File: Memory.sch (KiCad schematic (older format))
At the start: 26 parts, among them U10 74LS05, U11 74HCT00, U12 74LS27, U13 74HC74, U14 74HC86, U2 AS6C4008-55PCN, U3 AS6C4008-55PCN, U4 AS6C4008-55PCN, U5 AS6C4008-55PCN, U6 74HCT00, U7 74LS32, U8 74LS32, U9 74LS05

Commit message: cleaning up a bit more
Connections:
- net +5V: now also U14.4; no longer JP5.3 (B), U11.12
- net GND: now also U11.12, U11.13; no longer U14.4, U14.5
- net ~RST: now also U14.5; no longer U11.13
- net at U14.6: now also U13.3 (C)
- net at U11.11: no longer U13.3 (C)
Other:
- moved on the sheet: BT1, D1, D2, JP1, JP2, JP3, JP5, JP6, JP7, JP8, R1, U10D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

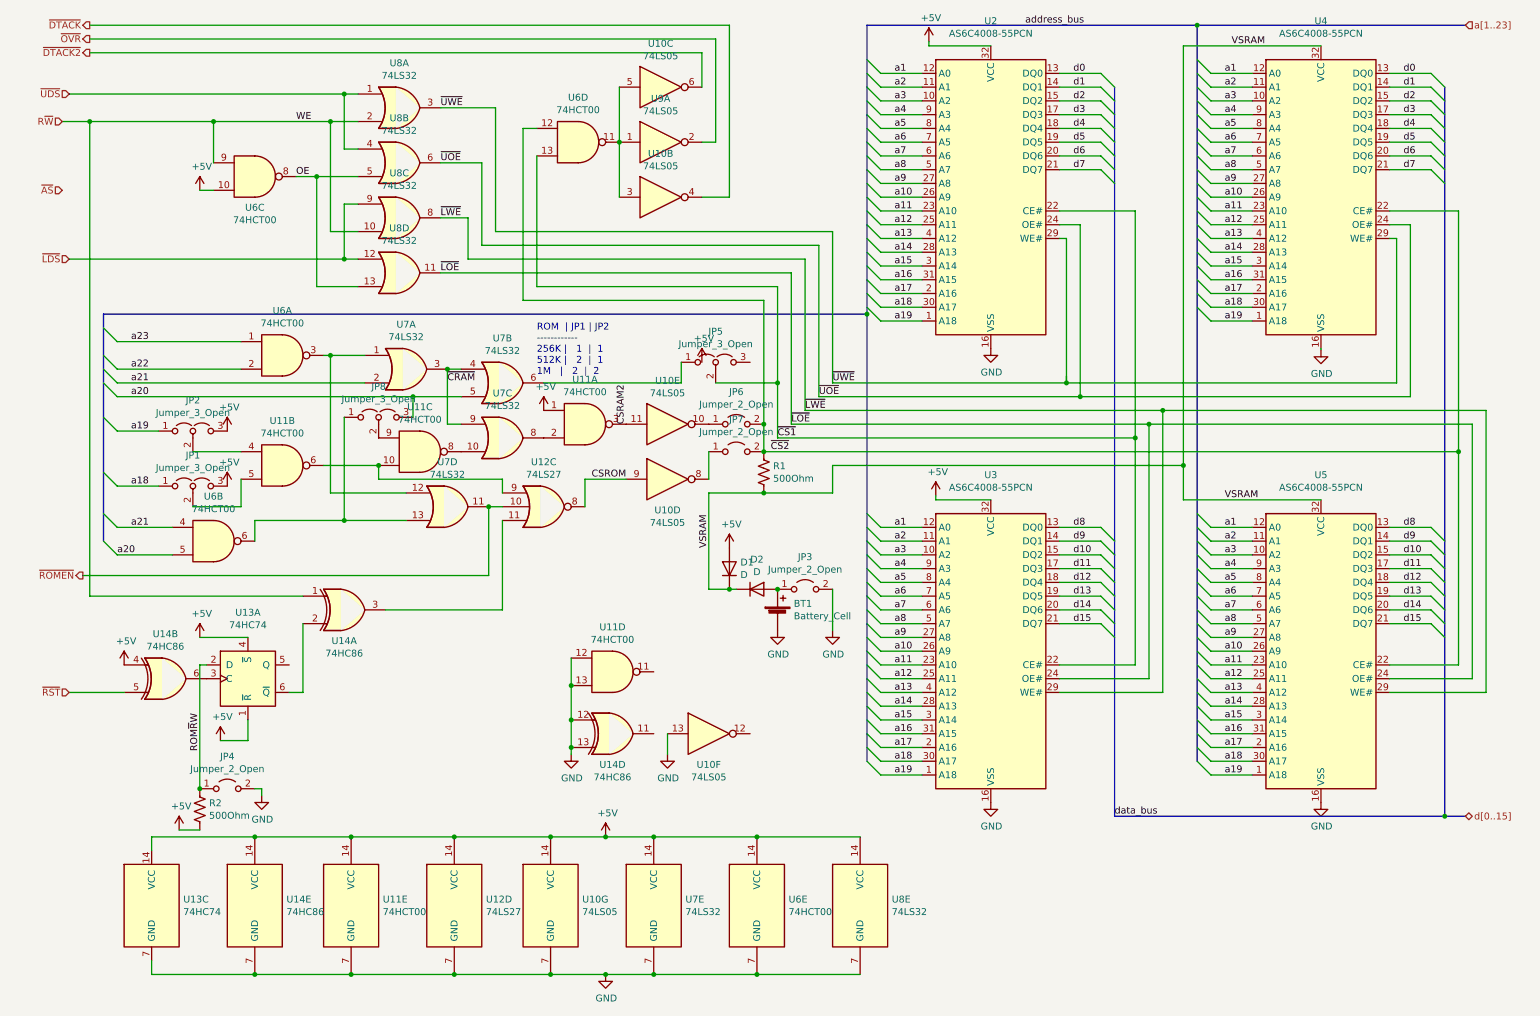
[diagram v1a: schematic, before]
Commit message: finish turbo section
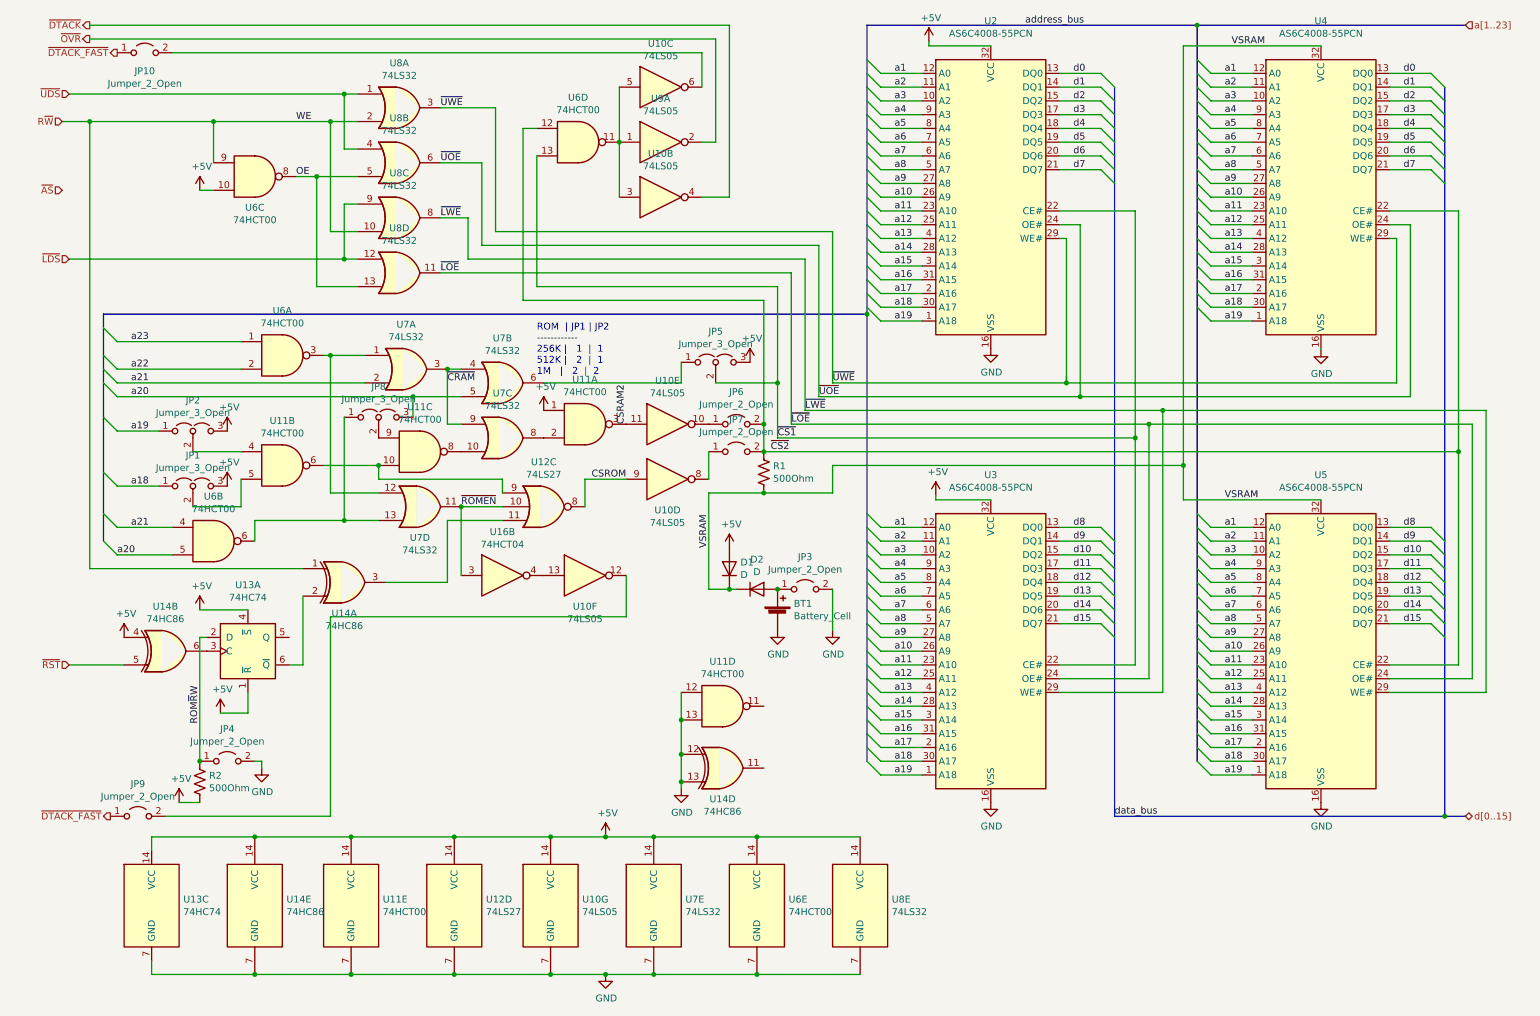
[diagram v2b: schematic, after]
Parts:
- added JP10, JP9: Jumper_2_Open, symbol jumper:Jumper_2_Open
- added U16: 74HCT04, symbol 74:74HCT04
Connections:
- net +5V: now also JP5.3 (B)
- net GND: no longer U10.13
- net ~ROMEN: now also U16.3
- net at U10.12: now also JP9.2 (B)
- net ~DTACK2: no longer names the net of U10.6
- net ~DTACK2: now also JP10.2 (B)
- new net: U10.13, U16.4
- new net ~DTACK_FAST: JP10.1 (A), JP9.1 (A)
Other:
- moved on the sheet: JP4, R2, U10F, U11D, U13A, U14A, U14B, U14D, U7D

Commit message: component names
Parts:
- JP1: value Jumper_3_Open -> 256K_512K
- JP10: value Jumper_2_Open -> Turbo_SRAM
- JP2: value Jumper_3_Open -> 512K_1MB
- JP3: value Jumper_2_Open -> Battery
- JP4: value Jumper_2_Open -> ROMEMUW~R
- JP5: value Jumper_3_Open -> Bank0_ON_OFF
- JP6: value Jumper_2_Open -> Bank1
- JP7: value Jumper_2_Open -> ROMEMU
- JP8: value Jumper_3_Open -> Bank2_C0_D0
- JP9: value Jumper_2_Open -> Turbo_ROM
- R1, R2: value 500Ohm -> 500
- U13: value 74HC74 -> 74HCT74
- U14: value 74HC86 -> 74F86
- U7, U8: value 74LS32 -> 74HCT32
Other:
- note added: "74F is only \nrequired \nfor Turbo"

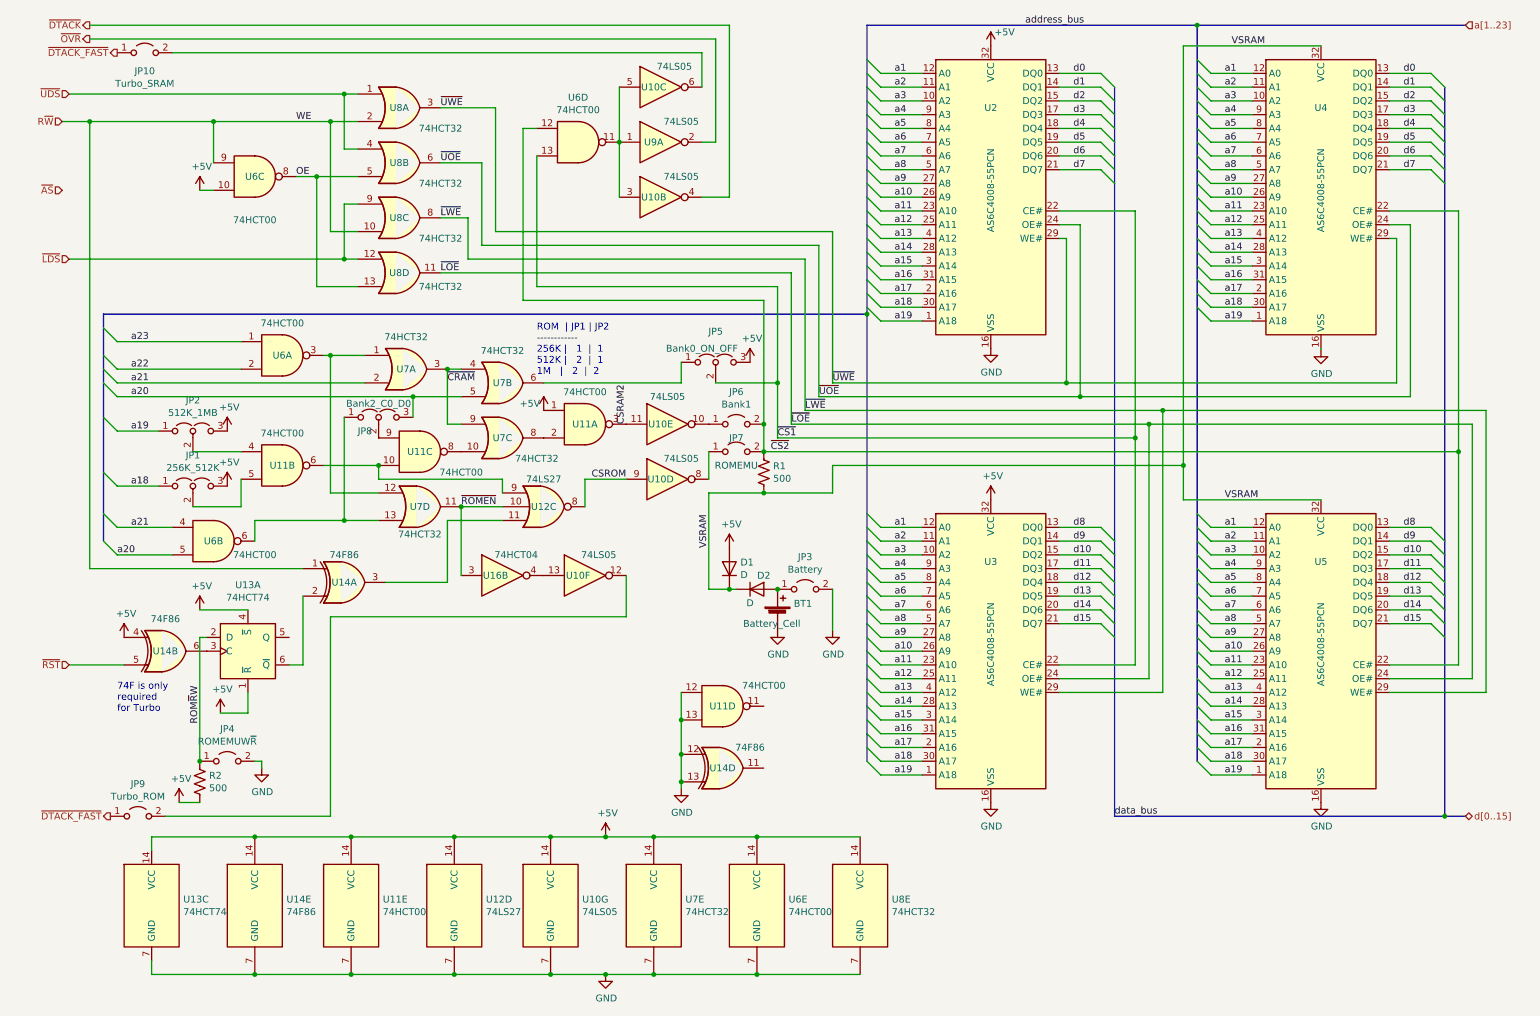
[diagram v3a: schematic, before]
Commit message: capacitors for memory
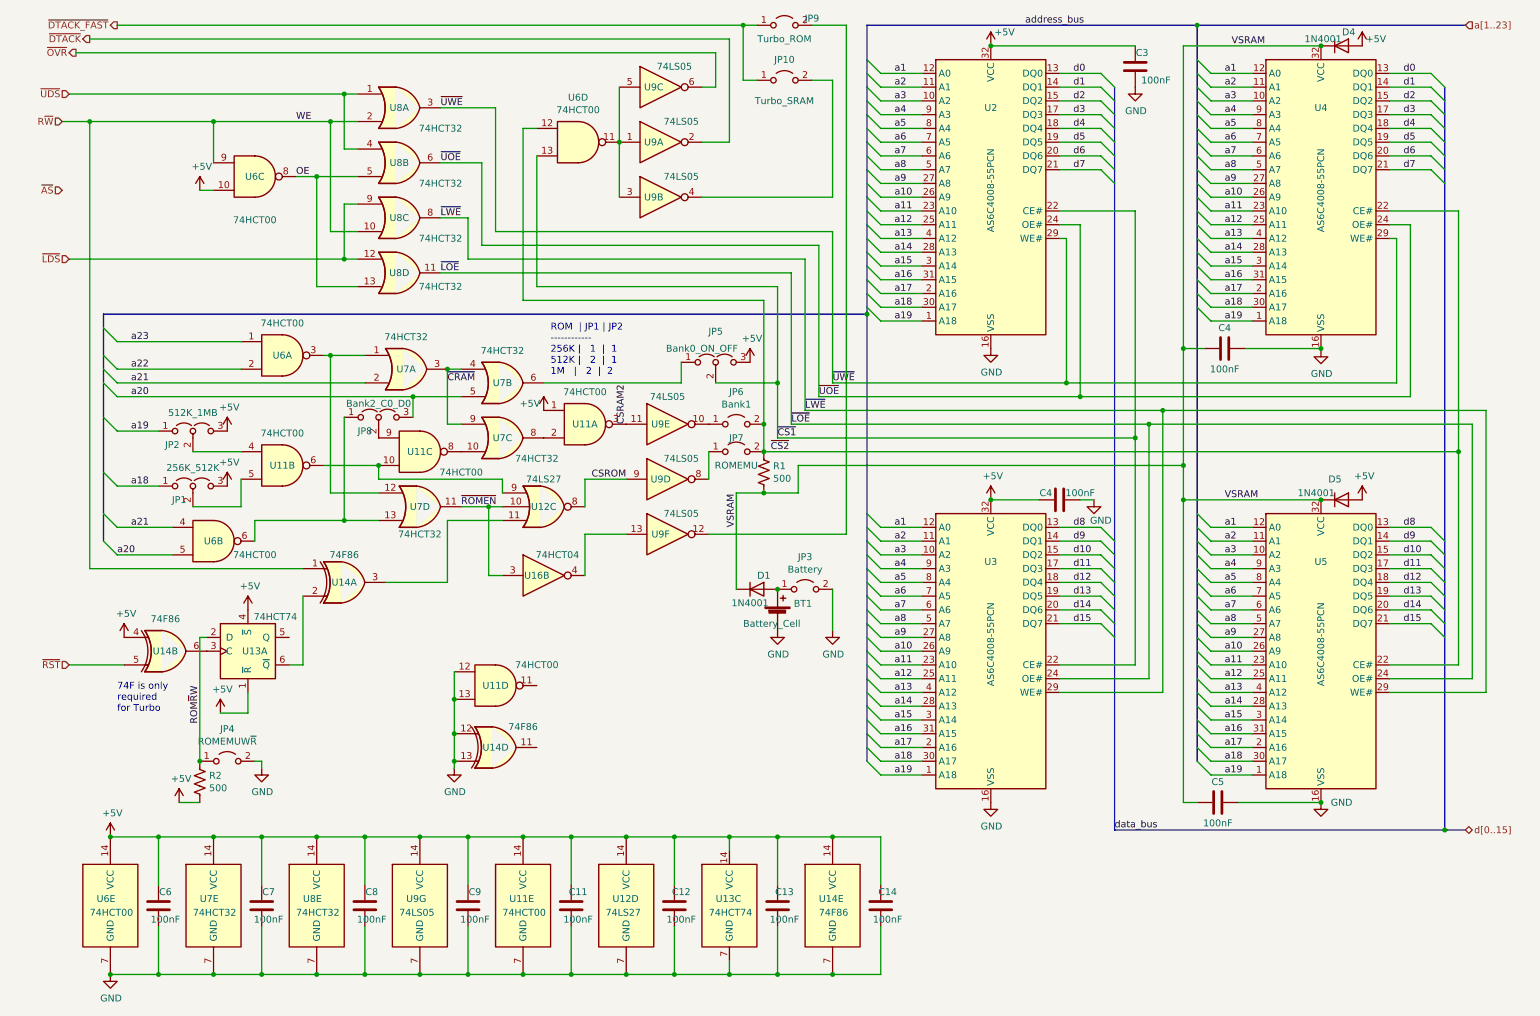
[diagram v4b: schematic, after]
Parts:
- added C11, C12, C13, C14, C3, C4 (x2), C5, C6, C7, C8, C9: 100nF, symbol device:C
- added D5: 1N4001, symbol device:D
- D1: renamed from D2; value D -> 1N4001
- D4: renamed from D1; value D -> 1N4001
- renumbered U10 to U9
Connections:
- net +5V: now also C11.1, C12.1, C13.1, C14.1, C3.1, C4.2, C6.1, C7.1, C8.1, C9.1, D5.2 (A)
- net GND: now also C11.2, C12.2, C13.2, C14.2, C3.2, C4.1, C4.1, C5.1, C6.2, C7.2, C8.2, C9.2
- net VSRAM: now also C4.2, C5.2, D5.1 (K)
- net ~DTACK: now also U9.2; no longer U9.4
- net ~OVR: now also U9.6; no longer U9.2
- net at JP10.2 (B): now also U9.4; no longer U9.6
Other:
- moved on the sheet: D4, JP10, JP9, U11D, U11E, U12D, U13C, U14D, U14E, U16B, U6E, U7E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

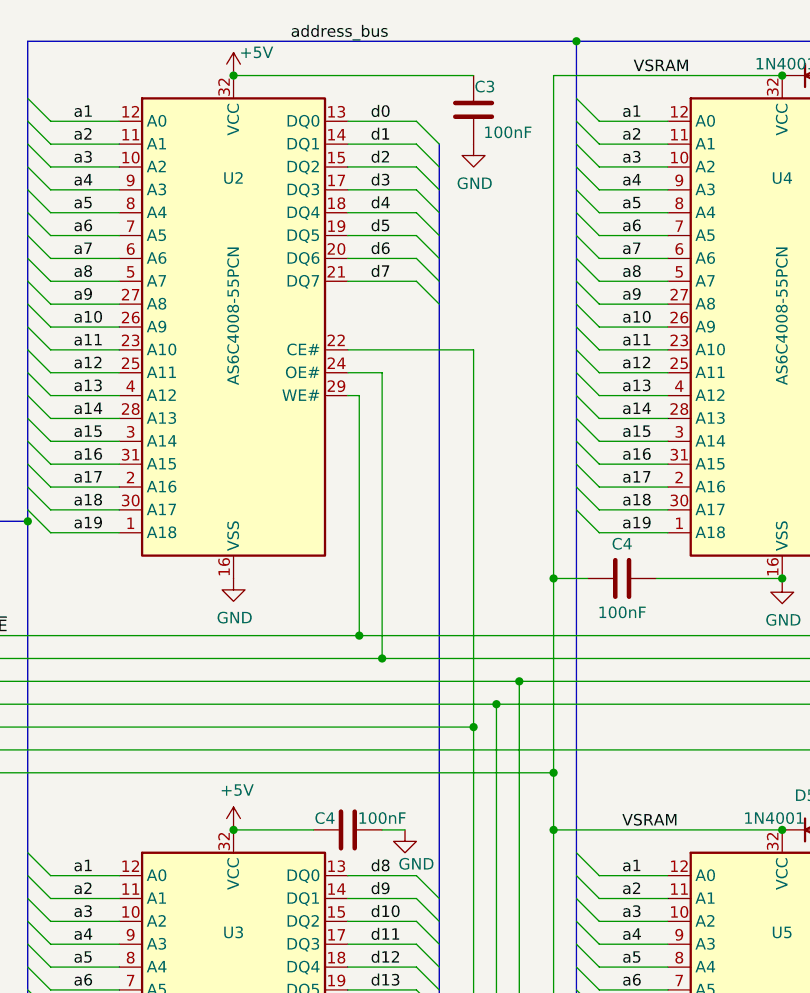
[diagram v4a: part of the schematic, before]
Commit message: add electrolytics
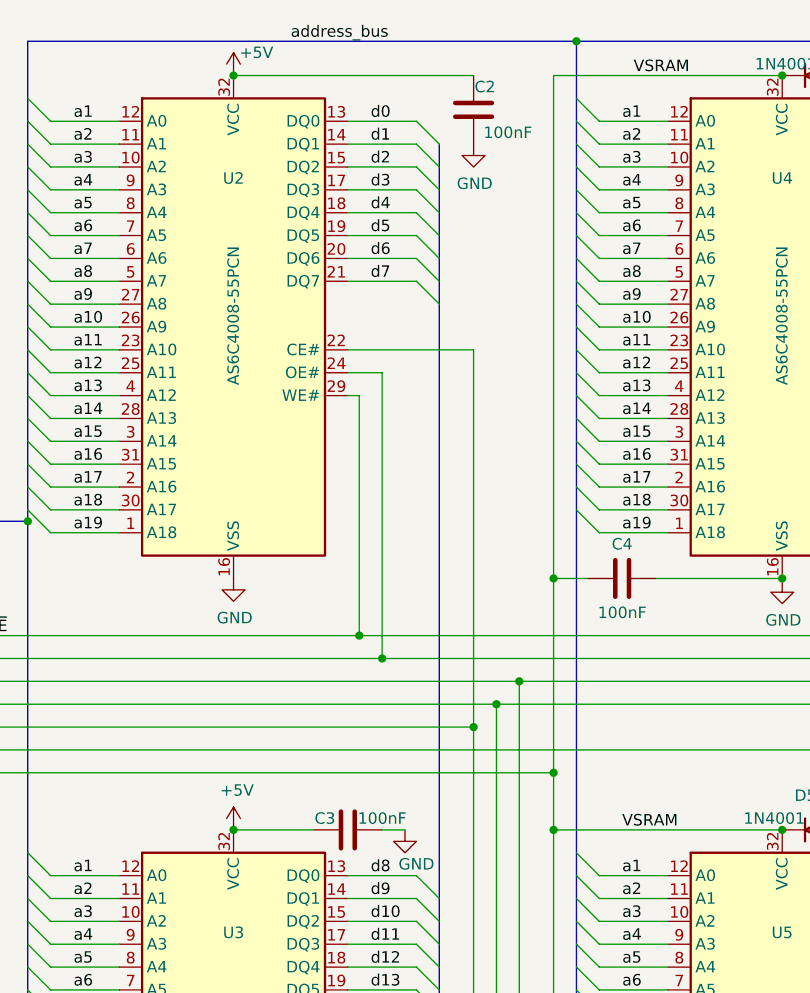
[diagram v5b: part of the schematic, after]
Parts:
- renumbered C3 to C2, C4 to C3
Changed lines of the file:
@@
 P 10100 4050
 AR Path="/6000A524" Ref="#PWR?"  Part="1"
-AR Path="/6068F728/6000A524" Ref="#PWR?"  Part="1"
-F 0 "#PWR?" H 10100 3900 50  0001 C CNN
+AR Path="/6068F728/6000A524" Ref="#PWR0138"  Part="1"
+F 0 "#PWR0138" H 10100 3900 50  0001 C CNN
 F 1 "+5V" H 10115 4223 50  0000 C CNN
 F 2 "" H 10100 4050 50  0001 C CNN
@@
 	5300 1850 6250 1850
 $Comp
-L device:C C3
+L device:C C2
 U 1 1 606D2308
 P 8450 900
-F 0 "C3" H 8500 1000 50  0000 C CNN
+F 0 "C2" H 8500 1000 50  0000 C CNN
 F 1 "100nF" H 8600 800 50  0000 C CNN
 F 2 "" H 8488 750 50  0001 C CNN
@@
 P 8450 1050
 AR Path="/6075FE5F" Ref="#PWR?"  Part="1"
-AR Path="/6068F728/6075FE5F" Ref="#PWR?"  Part="1"
-F 0 "#PWR?" H 8450 800 50  0001 C CNN
+AR Path="/6068F728/6075FE5F" Ref="#PWR0139"  Part="1"
+F 0 "#PWR0139" H 8450 800 50  0001 C CNN
 F 1 "GND" H 8455 877 50  0000 C CNN
 F 2 "" H 8450 1050 50  0001 C CNN
@@
 $EndComp
 $Comp
-L device:C C4
+L device:C C3
 U 1 1 6076112A
 P 7900 4050
-F 0 "C4" V 7850 3950 50  0000 C CNN
+F 0 "C3" V 7850 3950 50  0000 C CNN
 F 1 "100nF" V 7850 4200 50  0000 C CNN
 F 2 "" H 7938 3900 50  0001 C CNN
@@
 P 8150 4050
 AR Path="/60789592" Ref="#PWR?"  Part="1"
-AR Path="/6068F728/60789592" Ref="#PWR?"  Part="1"
-F 0 "#PWR?" H 8150 3800 50  0001 C CNN
+AR Path="/6068F728/60789592" Ref="#PWR0140"  Part="1"
+F 0 "#PWR0140" H 8150 3800 50  0001 C CNN
 F 1 "GND" H 8200 3900 50  0000 C CNN
 F 2 "" H 8150 4050 50  0001 C CNN

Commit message: sheet metadata
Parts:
- U12: value 74LS27 -> 74HCT27
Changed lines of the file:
@@
 encoding utf-8
 Sheet 2 3
-Title ""
+Title "Ranger RAM"
 Date ""
 Rev ""
-Comp ""
+Comp "Jan Hofmeier"
 Comment1 ""
 Comment2 ""
@@
 P 4150 4100
 F 0 "U12" H 4150 4100 50  0000 C CNN
-F 1 "74LS27" H 4150 4300 50  0000 C CNN
+F 1 "74HCT27" H 4150 4300 50  0000 C CNN
 F 2 "" H 4150 4100 50  0001 C CNN
 F 3 "http://www.ti.com/lit/gpn/sn74LS27" H 4150 4100 50  0001 C CNN
@@
 P 4750 7000
 F 0 "U12" H 4650 7050 50  0000 L CNN
-F 1 "74LS27" H 4600 6950 50  0000 L CNN
+F 1 "74HCT27" H 4600 6950 50  0000 L CNN
 F 2 "" H 4750 7000 50  0001 C CNN
 F 3 "http://www.ti.com/lit/gpn/sn74LS27" H 4750 7000 50  0001 C CNN

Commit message: assign footprints
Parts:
- BT1: footprint (none) -> Battery:BatteryHolder_Keystone_103_1x20mm
- C11, C12, C13, C14, C2, C3, C4, C5, C6, C7, C8, C9: footprint (none) -> Capacitor_THT:C_Disc_D7.0mm_W2.5mm_P5.00mm
- D1, D4, D5: footprint (none) -> Diode_THT:D_A-405_P7.62mm_Horizontal
- JP1, JP2, JP8: footprint (none) -> Connector_PinHeader_2.54mm:PinHeader_1x03_P2.54mm_Vertical
- JP10, JP3, JP4, JP7, JP9: footprint (none) -> Connector_PinHeader_2.54mm:PinHeader_1x02_P2.54mm_Vertical
- JP5: value Bank0_ON_OFF -> Bank1_ON_OFF; footprint (none) -> Connector_PinHeader_2.54mm:PinHeader_1x03_P2.54mm_Vertical
- JP6: value Bank1 -> Bank2; footprint (none) -> Connector_PinHeader_2.54mm:PinHeader_1x02_P2.54mm_Vertical
- R1, R2: footprint (none) -> Resistor_THT:R_Axial_DIN0411_L9.9mm_D3.6mm_P12.70mm_Horizontal
- U11, U12, U13, U16, U6, U7, U8, U9: footprint (none) -> Package_DIP:DIP-14_W7.62mm
- U14: footprint (none) -> Package_DIP:DIP-14_W7.62mm_Socket
- U2, U3, U4, U5: footprint Package_DIP:DIP-32_W15.24mm -> Package_DIP:DIP-32_W15.24mm_Socket
